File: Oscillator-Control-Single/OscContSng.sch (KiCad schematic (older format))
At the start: 59 parts, among them J1 CortexM_Debug, J3 USB_OTG, SW1 Waveform, SW11 Release, SW4 Attack, SW5 Decay, SW9 Sustain, U1 AZ1117-3.3, U2 SAMD20E15A-AU, Y1 32.768kHz

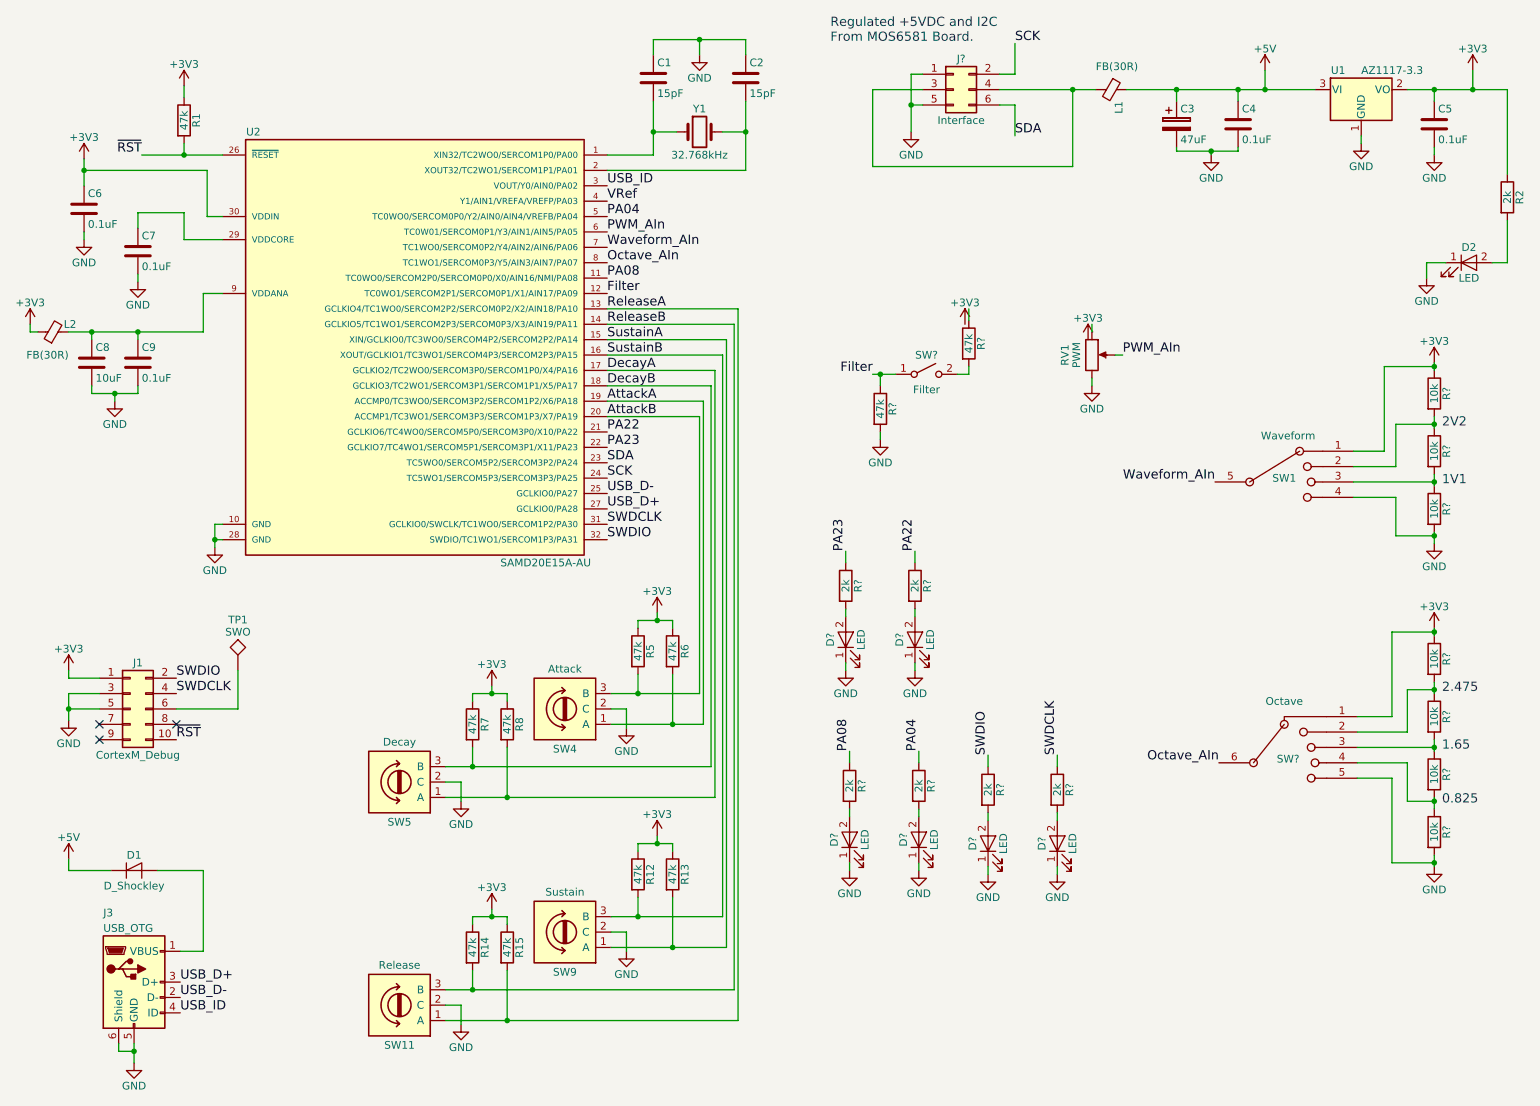
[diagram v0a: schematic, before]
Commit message: added i2c address switch to osc board design.
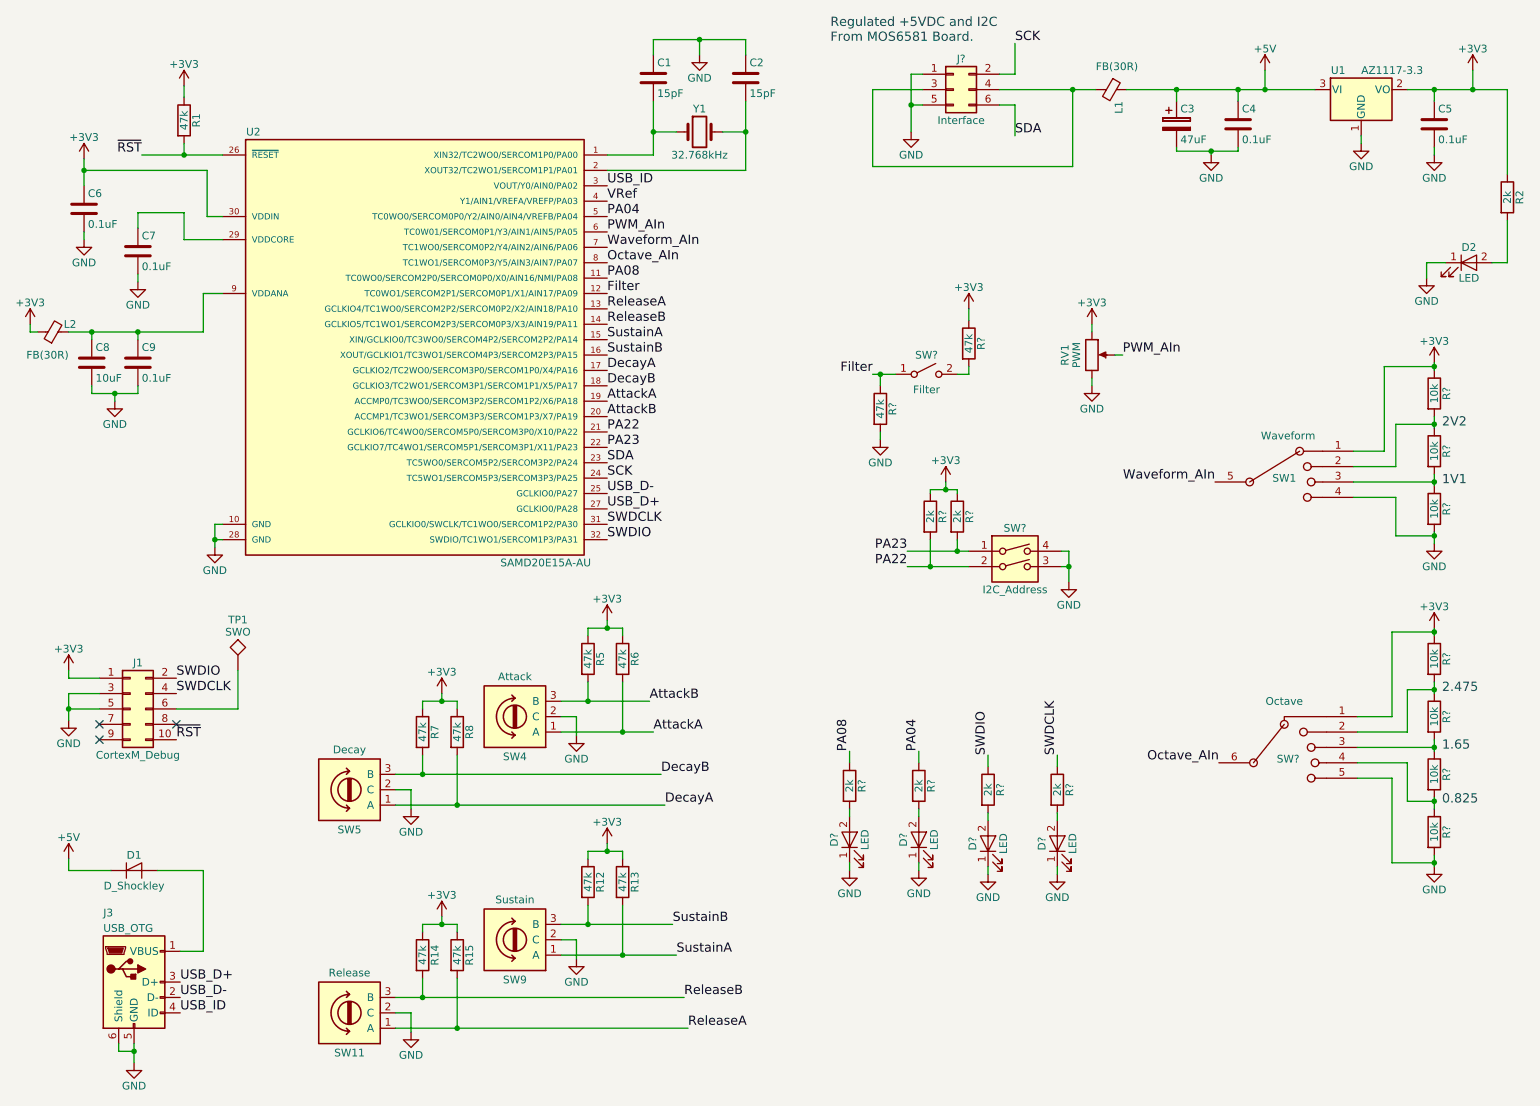
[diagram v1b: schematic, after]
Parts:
- removed D? (x2): LED, symbol LED
- added SW?: I2C_Address, symbol SW_DIP_x02
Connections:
- net +3V3: now also R?.1, R?.1, R?.1, RV1.1
- net GND: now also SW?.3, SW?.4
- net PA22: now also R?.2, SW?.2; no longer R?.1
- net PA23: now also R?.2, SW?.1; no longer R?.1
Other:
- moved on the sheet: R12, R13, R14, R15, R5, R6, R7, R8, R?, SW11, SW4, SW5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

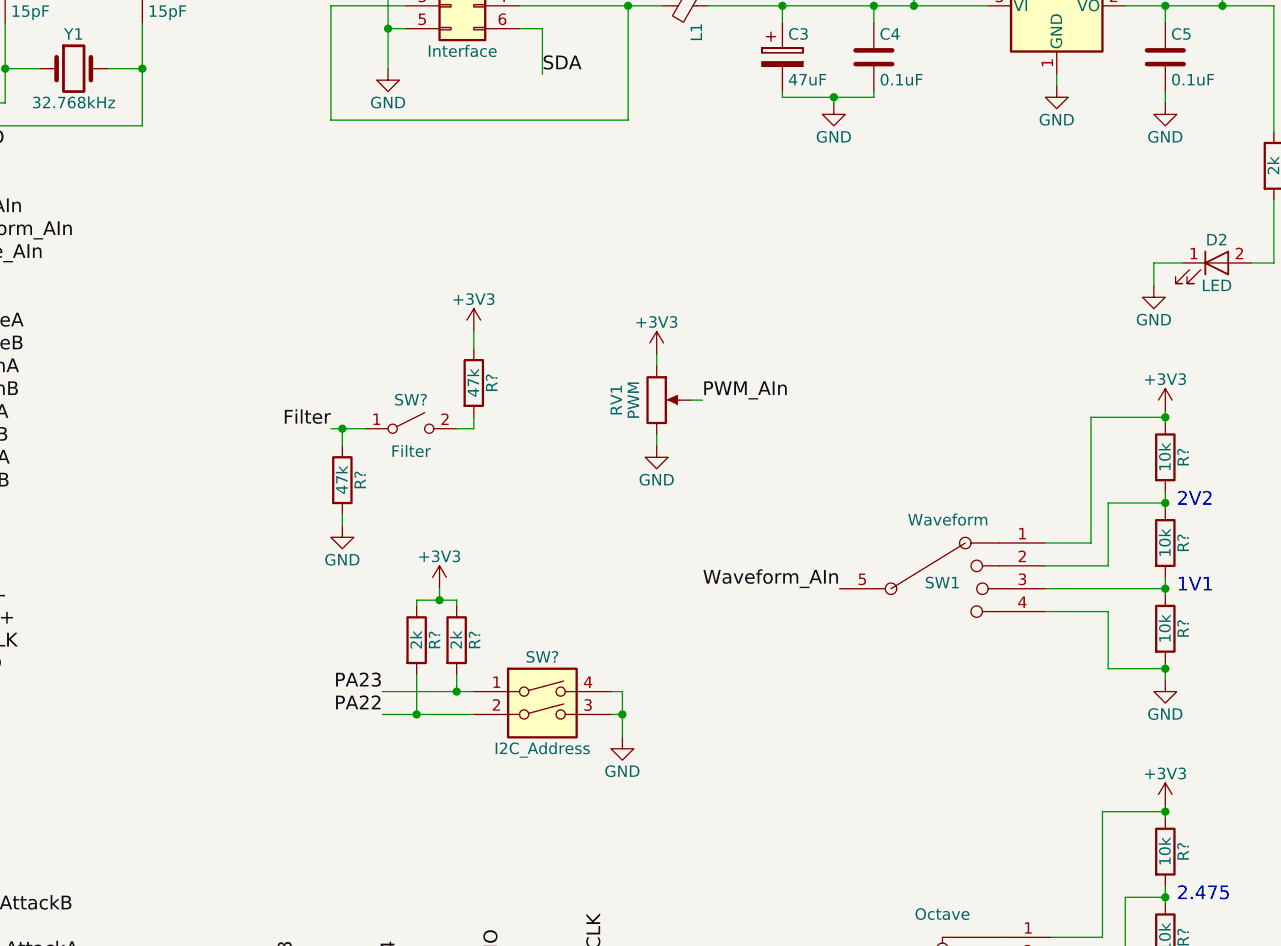
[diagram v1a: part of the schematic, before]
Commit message: osc schematic touchup.
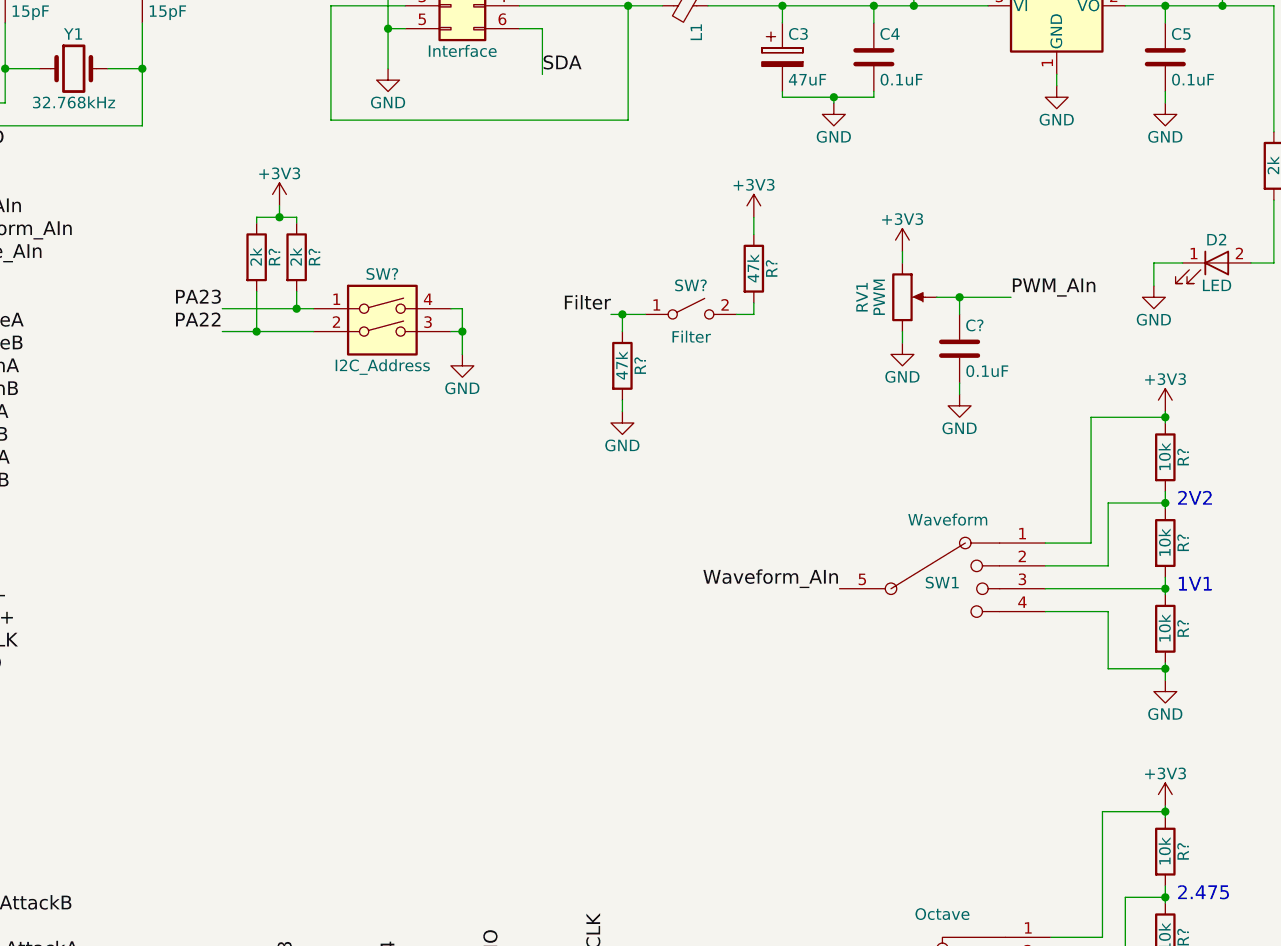
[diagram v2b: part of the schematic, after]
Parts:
- added C?: 0.1uF, symbol C
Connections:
- net GND: now also C?.2
- net PWM_AIn: now also C?.1
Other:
- moved on the sheet: R?, RV1, SW?

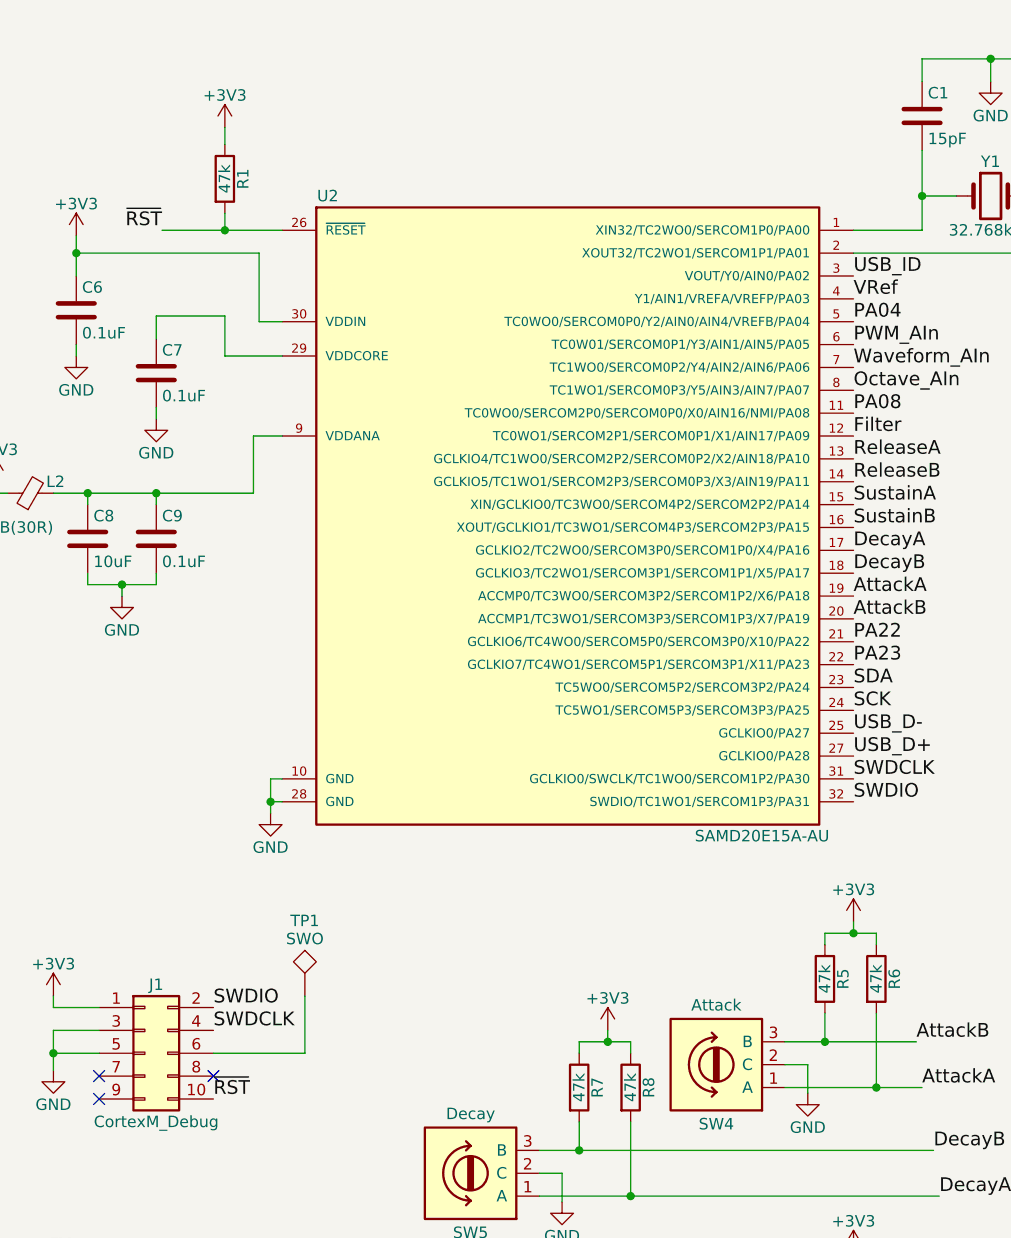
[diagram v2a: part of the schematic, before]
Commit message: added pullups and caps in various places on osc sch.
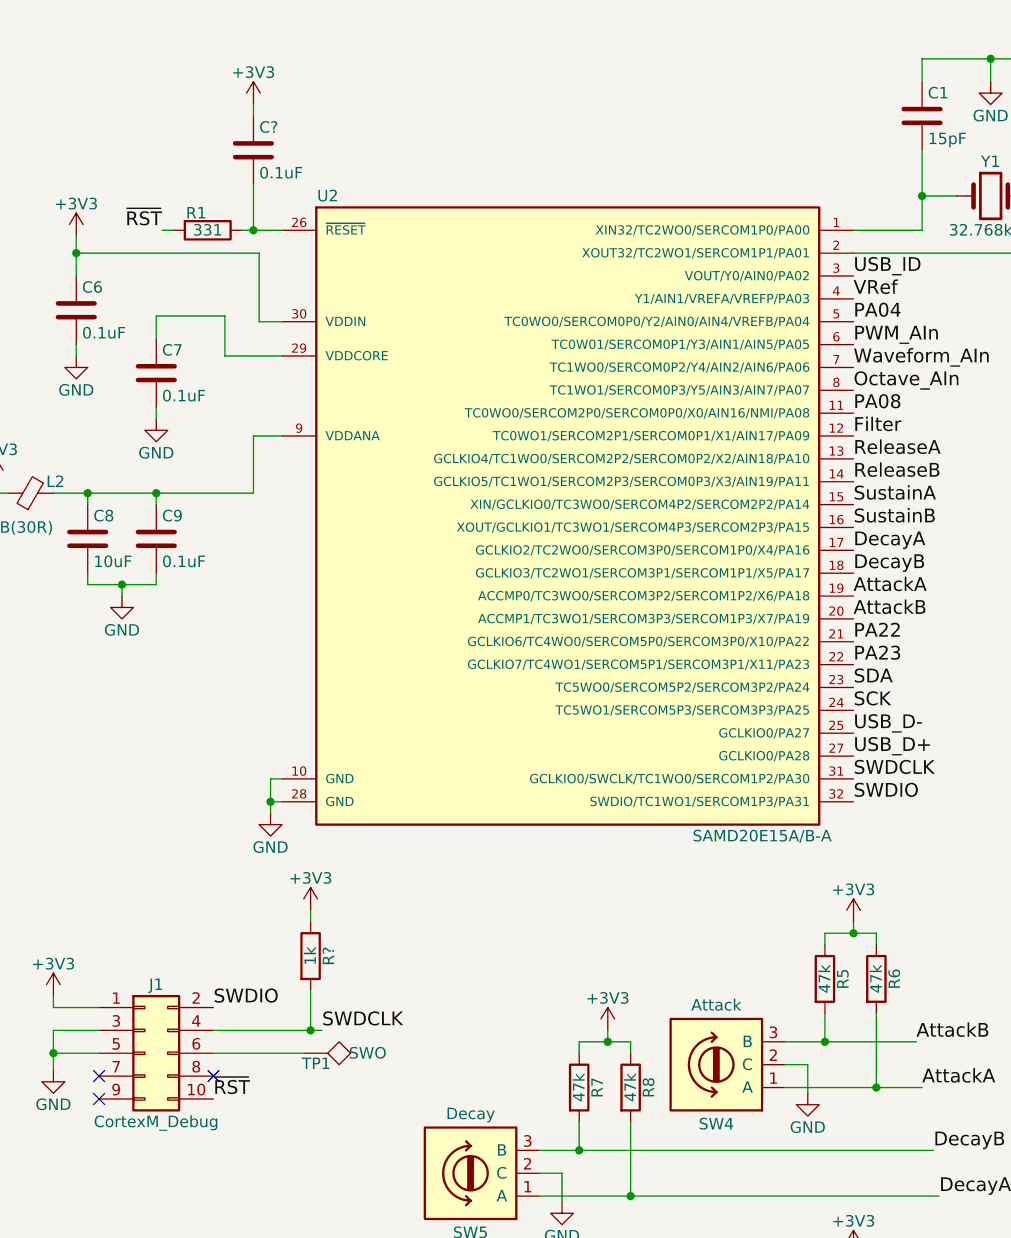
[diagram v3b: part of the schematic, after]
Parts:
- added C?: 0.1uF, symbol C
- added R?: 1k, symbol R
- R1: value 47k -> 331
- U2: value SAMD20E15A-AU -> SAMD20E15A/B-A; footprint TQFP32 -> Housings_QFP:TQFP-32_7x7mm_Pitch0.8mm; Critical (none) -> N; Description (none) -> IC MCU 32BIT 32KB FLASH 32TQFP; Source (none) -> 1611-ATSAMD21E15B-AFTCT-ND; VPN (none) -> ATSAMD21E15B-AFT
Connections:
- net +3V3: now also C?.1, R?.1; no longer R1.1
- net SWDCLK: now also R?.2
- net ~RST: no longer U2.26 (~RESET~)
- new net: C?.2, R1.1, U2.26 (~RESET~)
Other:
- moved on the sheet: R1, TP1
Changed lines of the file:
@@
 L +3V3 #PWR9
 U 1 1 5C2115A3
-P 1725 1100
-F 0 "#PWR9" H 1725 950 50  0001 C CNN
-F 1 "+3V3" H 1725 1240 50  0000 C CNN
-F 2 "" H 1725 1100 50  0001 C CNN
-F 3 "" H 1725 1100 50  0001 C CNN
-	1    1725 1100
+P 1850 1000
+F 0 "#PWR9" H 1850 850 50  0001 C CNN
+F 1 "+3V3" H 1850 1140 50  0000 C CNN
+F 2 "" H 1850 1000 50  0001 C CNN
+F 3 "" H 1850 1000 50  0001 C CNN
+	1    1850 1000
 	1    0    0    -1
 $EndComp
@@
 L R R1
 U 1 1 5C212460
-P 1725 1325
-F 0 "R1" V 1805 1325 50  0000 C CNN
-F 1 "47k" V 1725 1325 50  0000 C CNN
-F 2 "" V 1655 1325 50  0001 C CNN
-F 3 "" H 1725 1325 50  0001 C CNN
-	1    1725 1325
-	1    0    0    -1
+P 1650 1550
+F 0 "R1" V 1575 1500 50  0000 C CNN
+F 1 "331" V 1650 1550 50  0000 C CNN
+F 2 "" V 1580 1550 50  0001 C CNN
+F 3 "" H 1650 1550 50  0001 C CNN
+	1    1650 1550
+	0    1    1    0
 $EndComp
 Text Label 4475 1950 0    60   ~ 0
@@
 Text Label 1675 4950 0    60   ~ 0
 SWDIO
-Text Label 1675 5050 0    60   ~ 0
+Text Label 2150 5050 0    60   ~ 0
 SWDCLK
 Text Label 1675 5350 0    60   ~ 0
@@
 Wire Wire Line
 	1675 5150 2075 5150
-Wire Wire Line
-	2075 5150 2075 4900
 $Comp
 L TEST TP1
 U 1 1 5C2143E1
-P 2075 4900
-F 0 "TP1" H 2075 5200 50  0000 C BNN
-F 1 "SWO" H 2075 5150 50  0000 C CNN
-F 2 "" H 2075 4900 50  0001 C CNN
-F 3 "" H 2075 4900 50  0001 C CNN
-	1    2075 4900
-	1    0    0    -1
+P 2075 5150
+F 0 "TP1" V 2150 5200 50  0000 C BNN
+F 1 "SWO" V 2075 5425 50  0000 C CNN
+F 2 "" H 2075 5150 50  0001 C CNN
+F 3 "" H 2075 5150 50  0001 C CNN
+	1    2075 5150
+	0    1    1    0
 $EndComp
 Text Label 4475 3450 0    60   ~ 0
@@
 P 3225 2800
 F 0 "U2" H 2175 4200 50  0000 C CNN
-F 1 "SAMD20E15A-AU" H 4075 1400 50  0000 C CNN
-F 2 "TQFP32" H 3225 1800 50  0001 C CIN
+F 1 "SAMD20E15A/B-A" H 4075 1400 50  0000 C CNN
+F 2 "Housings_QFP:TQFP-32_7x7mm_Pitch0.8mm" H 3225 1800 50  0001 C CIN
 F 3 "" H 3225 2800 50  0001 C CNN
+F 4 "~" H 3225 2800 60  0000 C CNN "Characteristics"
+F 5 "IC MCU 32BIT 32KB FLASH 32TQFP" H 3225 2800 60  0001 C CNN "Description"
+F 6 "~" H 3225 2800 60  0001 C CNN "VName"
+F 7 "ATSAMD21E15B-AFT" H 3225 2800 60  0001 C CNN "VPN"
+F 8 "~" H 3225 2800 60  0001 C CNN "PackaageID"
+F 9 "1611-ATSAMD21E15B-AFTCT-ND" H 3225 2800 60  0001 C CNN "Source"
+F 10 "N" H 3225 2800 60  0001 C CNN "Critical"
+F 11 "~" H 3225 2800 60  0001 C CNN "Notes"
 	1    3225 2800
 	1    0    0    -1
 $EndComp
-Wire Wire Line
-	1450 1550 1975 1550
-Wire Wire Line
-	1725 1475 1725 1550
-Connection ~ 1725 1550
 Wire Wire Line
 	1075 1650 1875 1650
@@
 Wire Wire Line
 	1725 2100 1975 2100
-Wire Wire Line
-	1725 1100 1725 1175
 $Comp
 L +3V3 #PWR12
@@
 Wire Wire Line
 	8950 2775 8950 2825
+$Comp
+L C C?
+U 1 1 5C27A8EE
+P 1850 1200
+F 0 "C?" H 1875 1300 50  0000 L CNN
+F 1 "0.1uF" H 1875 1100 50  0000 L CNN
+F 2 "" H 1888 1050 50  0001 C CNN
+F 3 "" H 1850 1200 50  0001 C CNN
+	1    1850 1200
+	1    0    0    -1
+$EndComp
+Wire Wire Line
+	1450 1550 1500 1550
+Wire Wire Line
+	1850 1350 1850 1550
+Wire Wire Line
+	1800 1550 1975 1550
+Connection ~ 1850 1550
+Wire Wire Line
+	1850 1000 1850 1050
+Wire Wire Line
+	1675 5050 2150 5050
+Wire Wire Line
+	2100 5050 2100 4875
+$Comp
+L R R?
+U 1 1 5C27C62E
+P 2100 4725
+F 0 "R?" V 2180 4725 50  0000 C CNN
+F 1 "1k" V 2100 4725 50  0000 C CNN
+F 2 "" V 2030 4725 50  0001 C CNN
+F 3 "" H 2100 4725 50  0001 C CNN
+	1    2100 4725
+	1    0    0    -1
+$EndComp
+Connection ~ 2100 5050
+Wire Wire Line
+	2100 4575 2100 4525
+$Comp
+L +3V3 #PWR?
+U 1 1 5C27CC85
+P 2100 4525
+F 0 "#PWR?" H 2100 4375 50  0001 C CNN
+F 1 "+3V3" H 2100 4665 50  0000 C CNN
+F 2 "" H 2100 4525 50  0001 C CNN
+F 3 "" H 2100 4525 50  0001 C CNN
+	1    2100 4525
+	1    0    0    -1
+$EndComp
 $EndSCHEMATC
